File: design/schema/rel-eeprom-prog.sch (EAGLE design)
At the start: 4 parts, among them IC2 74HC595N, IC3 74HC595N

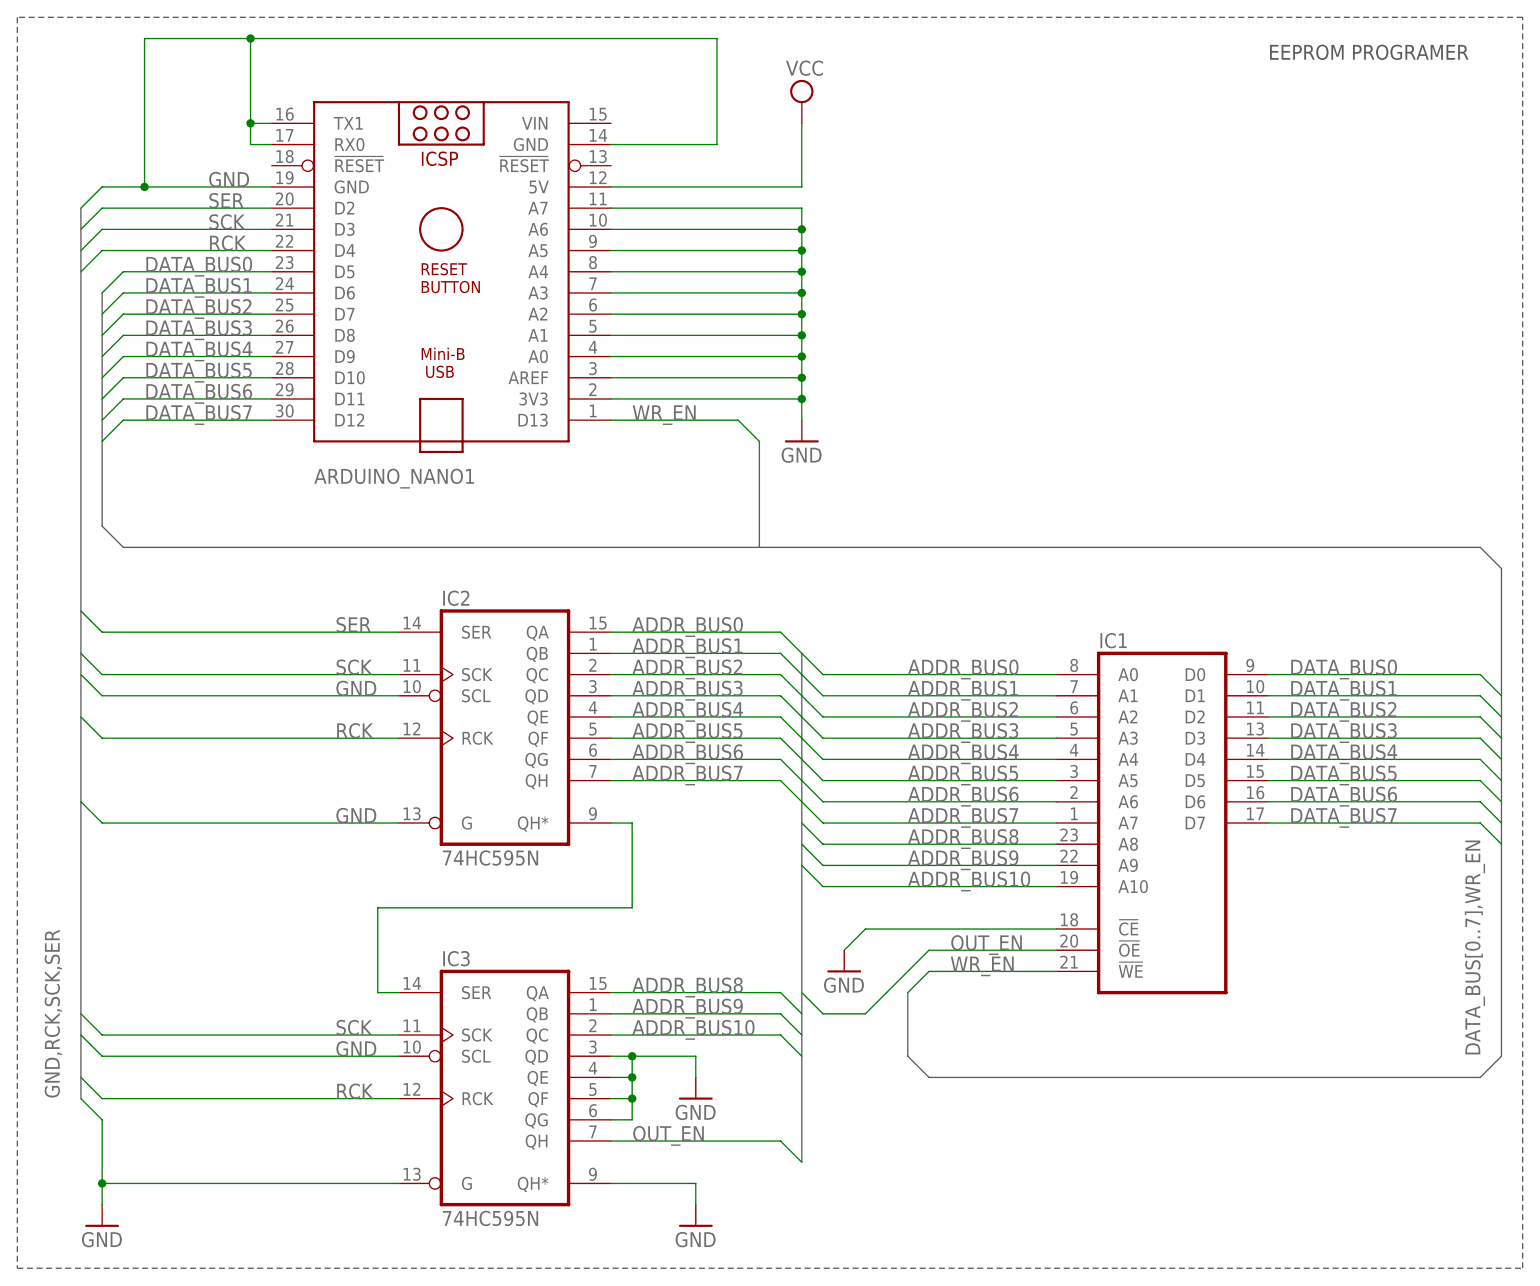
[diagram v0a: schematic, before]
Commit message: Fixed for improper pull down on SCL pin
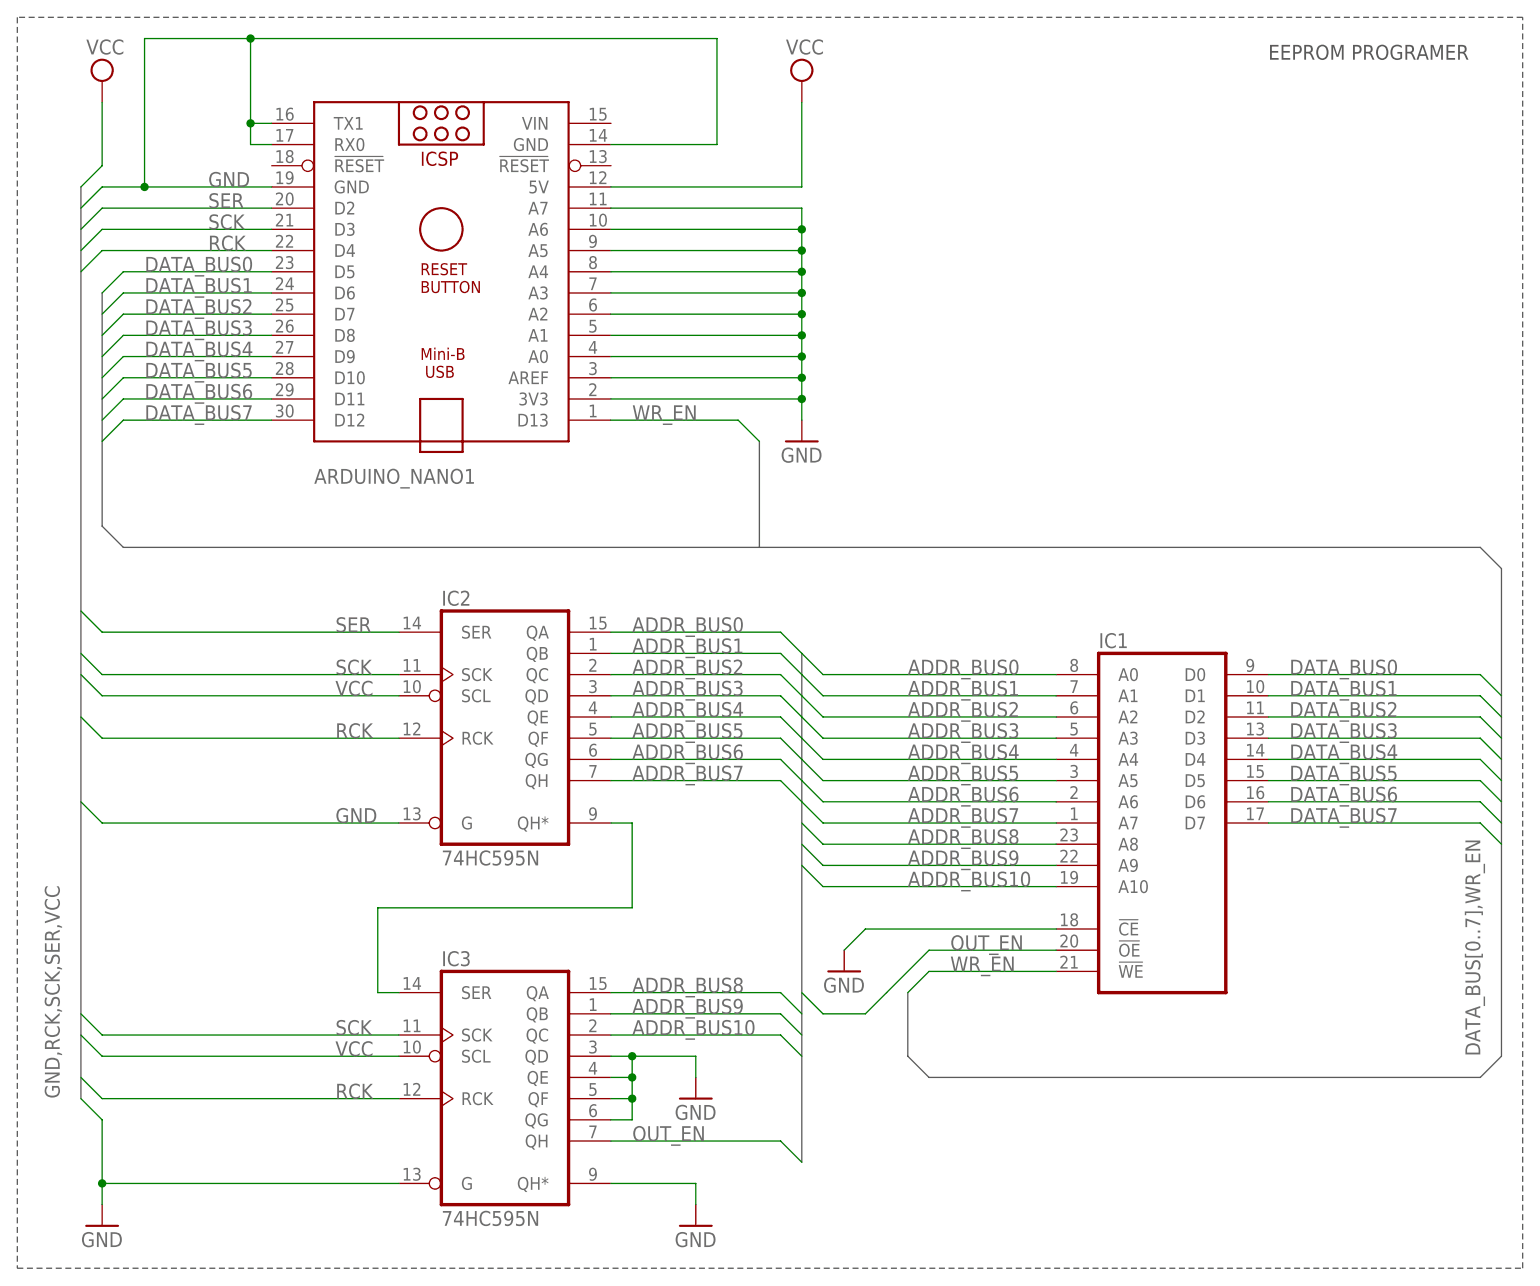
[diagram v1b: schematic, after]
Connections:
- net GND: no longer IC2A.SCL, IC3A.SCL
- net VCC: now also IC2A.SCL, IC3A.SCL
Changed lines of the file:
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@@
 <part name="GND1" library="supply1" library_urn="urn:adsk.eagle:library:371" deviceset="GND" device=""/>
 <part name="GND5" library="supply1" library_urn="urn:adsk.eagle:library:371" deviceset="GND" device=""/>
+<part name="SUPPLY2" library="supply2" library_urn="urn:adsk.eagle:library:372" deviceset="VCC" device=""/>
 </parts>
 <sheets>
@@
 <instance part="GND3" gate="1" x="63.5" y="12.7"/>
 <instance part="GND4" gate="1" x="45.72" y="-17.78"/>
-<instance part="SUPPLY1" gate="G$1" x="58.42" y="116.84"/>
+<instance part="SUPPLY1" gate="G$1" x="58.42" y="119.38"/>
 <instance part="GND1" gate="1" x="58.42" y="76.2"/>
 <instance part="GND5" gate="1" x="45.72" y="-2.54"/>
+<instance part="SUPPLY2" gate="G$1" x="-25.4" y="119.38"/>
 </instances>
 <busses>
-<bus name="GND,RCK,SCK,SER">
-<segment>
-<wire x1="-27.94" y1="104.14" x2="-27.94" y2="-2.54" width="0.762" layer="92"/>
+<bus name="GND,RCK,SCK,SER,VCC">
+<segment>
+<wire x1="-27.94" y1="106.68" x2="-27.94" y2="-2.54" width="0.762" layer="92"/>
 <label x="-30.48" y="-2.54" size="1.778" layer="95" rot="R90"/>
 </segment>
@@
 <wire x1="10.16" y1="-12.7" x2="-25.4" y2="-12.7" width="0.1524" layer="91"/>
 <junction x="-25.4" y="-12.7"/>
-</segment>
-<segment>
-<wire x1="-27.94" y1="48.26" x2="-25.4" y2="45.72" width="0.1524" layer="91"/>
-<pinref part="IC2" gate="A" pin="SCL"/>
-<wire x1="-25.4" y1="45.72" x2="10.16" y2="45.72" width="0.1524" layer="91"/>
-<label x="2.54" y="45.72" size="1.778" layer="95"/>
-</segment>
-<segment>
-<wire x1="-27.94" y1="5.08" x2="-25.4" y2="2.54" width="0.1524" layer="91"/>
-<pinref part="IC3" gate="A" pin="SCL"/>
-<wire x1="-25.4" y1="2.54" x2="10.16" y2="2.54" width="0.1524" layer="91"/>
-<label x="2.54" y="2.54" size="1.778" layer="95"/>
 </segment>
 <segment>
@@
 <wire x1="35.56" y1="106.68" x2="58.42" y2="106.68" width="0.1524" layer="91"/>
 <pinref part="SUPPLY1" gate="G$1" pin="VCC"/>
-<wire x1="58.42" y1="106.68" x2="58.42" y2="114.3" width="0.1524" layer="91"/>
-</segment>
-</net>
+<wire x1="58.42" y1="106.68" x2="58.42" y2="116.84" width="0.1524" layer="91"/>
+</segment>
+<segment>
+<wire x1="-27.94" y1="48.26" x2="-25.4" y2="45.72" width="0.1524" layer="91"/>
+<pinref part="IC2" gate="A" pin="SCL"/>
+<wire x1="-25.4" y1="45.72" x2="10.16" y2="45.72" width="0.1524" layer="91"/>
+<label x="2.54" y="45.72" size="1.778" layer="95"/>
+</segment>
+<segment>
+<wire x1="-27.94" y1="5.08" x2="-25.4" y2="2.54" width="0.1524" layer="91"/>
+<pinref part="IC3" gate="A" pin="SCL"/>
+<wire x1="-25.4" y1="2.54" x2="10.16" y2="2.54" width="0.1524" layer="91"/>
+<label x="2.54" y="2.54" size="1.778" layer="95"/>
+</segment>
+<segment>
+<wire x1="-27.94" y1="106.68" x2="-25.4" y2="109.22" width="0.1524" layer="91"/>
+<wire x1="-25.4" y1="109.22" x2="-25.4" y2="116.84" width="0.1524" layer="91"/>
+<pinref part="SUPPLY2" gate="G$1" pin="VCC"/>
+</segment>
+</net>

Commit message: Added initial version of board design
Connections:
- net N$17 renamed CARRY
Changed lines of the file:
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@@
 </segment>
 </net>
-<net name="N$17" class="0">
+<net name="CARRY" class="0">
 <segment>
 <pinref part="IC2" gate="A" pin="QH*"/>

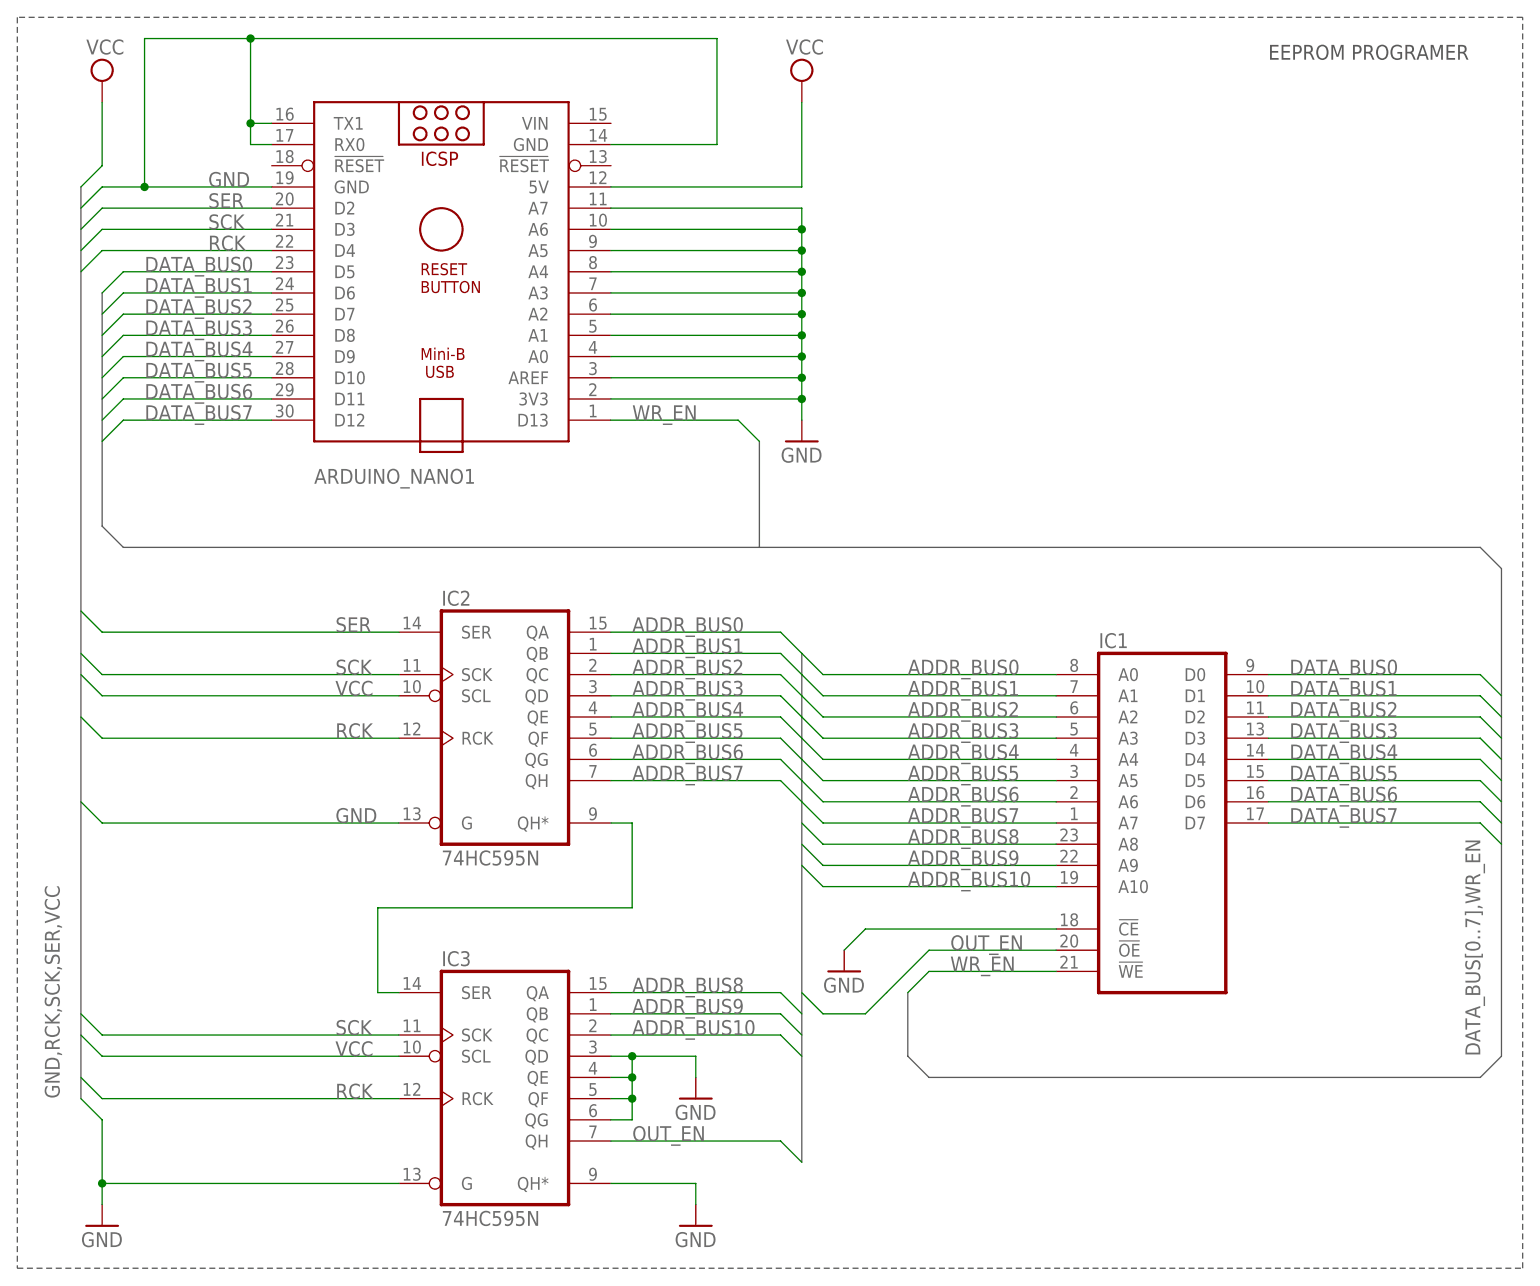
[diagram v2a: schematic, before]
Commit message: Updated IC chips names
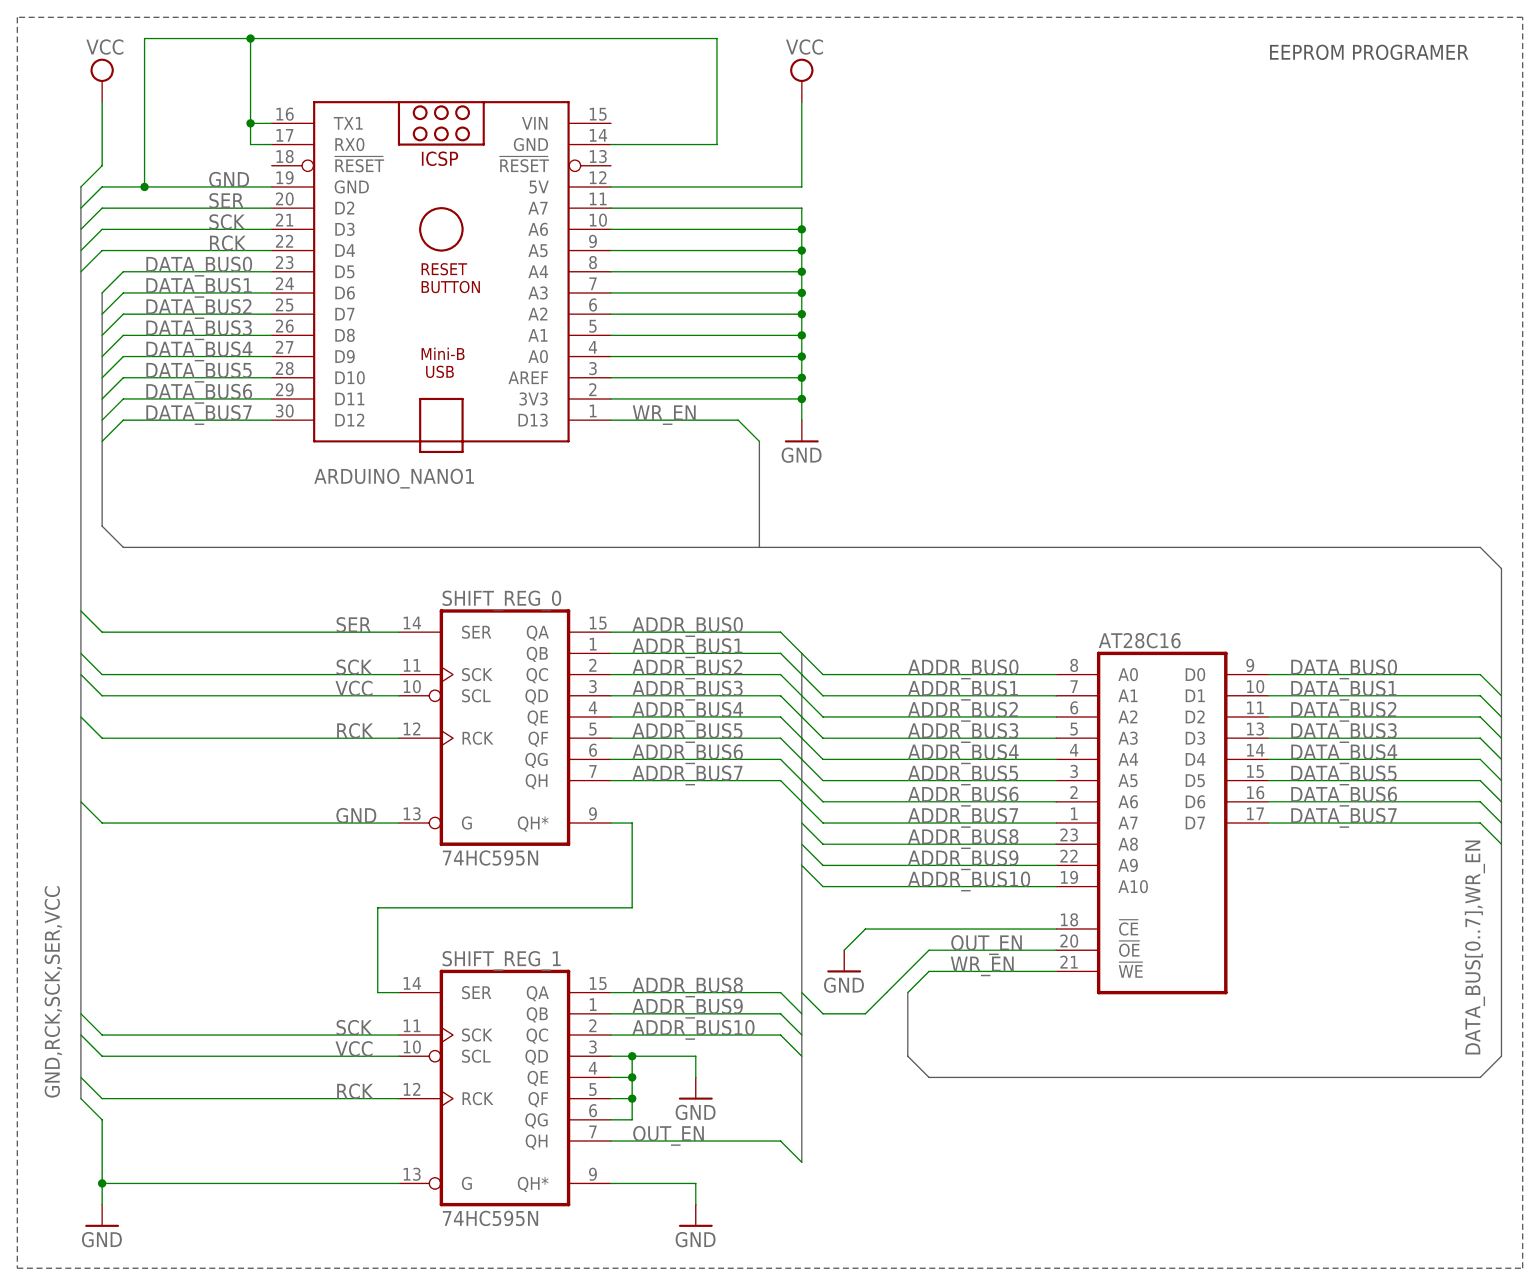
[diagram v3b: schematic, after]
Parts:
- renumbered IC1 to AT28C16, IC2 to SHIFT_REG_0, IC3 to SHIFT_REG_1
